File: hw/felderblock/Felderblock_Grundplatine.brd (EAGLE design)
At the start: 100 x 80 mm, 52 parts, among them IC2 LM2936, IC3 ULN2803, IC4 MCP2300X/P, J1 RJ11, J2 RJ11, M1 ARDUINO-NANO-3.0, T2 BC337, X1 TASTENSPERRE1, X2 TASTENSPERRE2, X3 SCHLUESSELSPERRE, X4 I2C, X5 ANSCHALTER

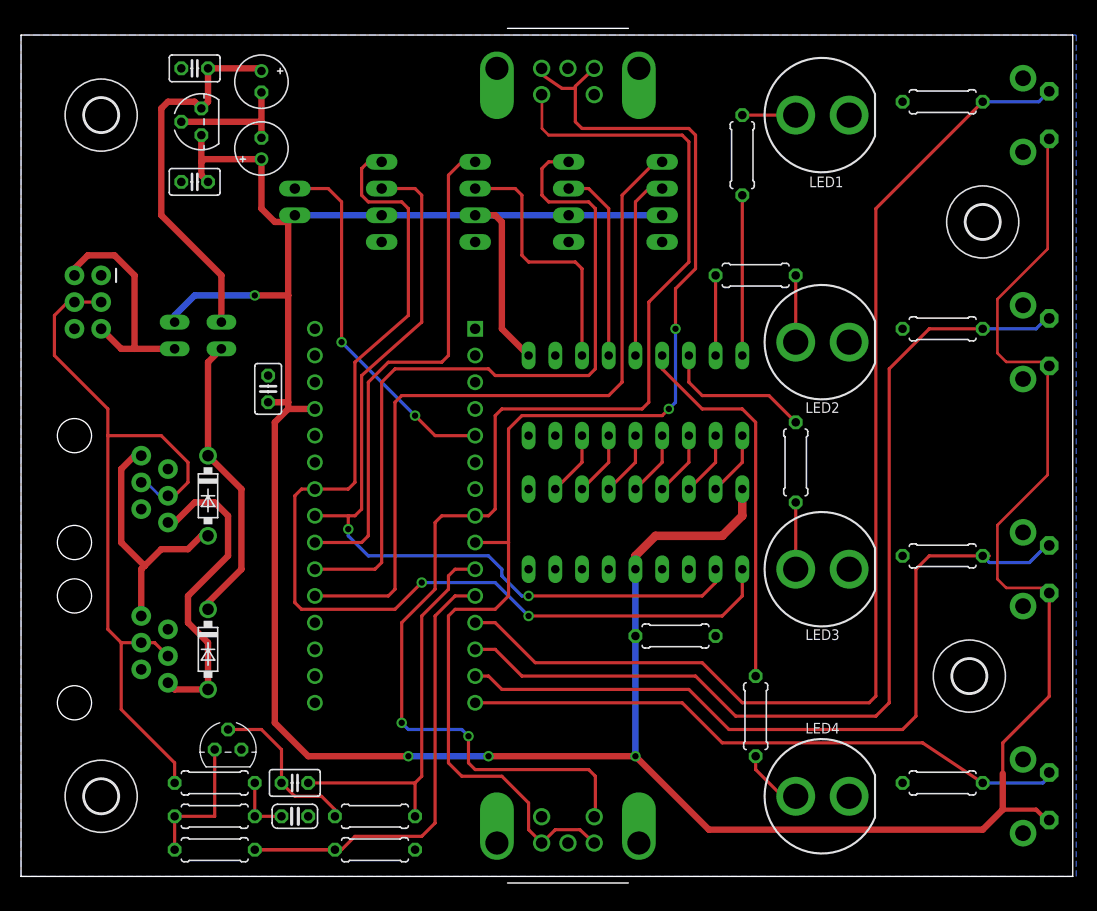
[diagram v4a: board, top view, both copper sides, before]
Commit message: position pcb into housing
restructure parts for housing, made pcb smaller to fit housing, positioned LED and buttons to fit
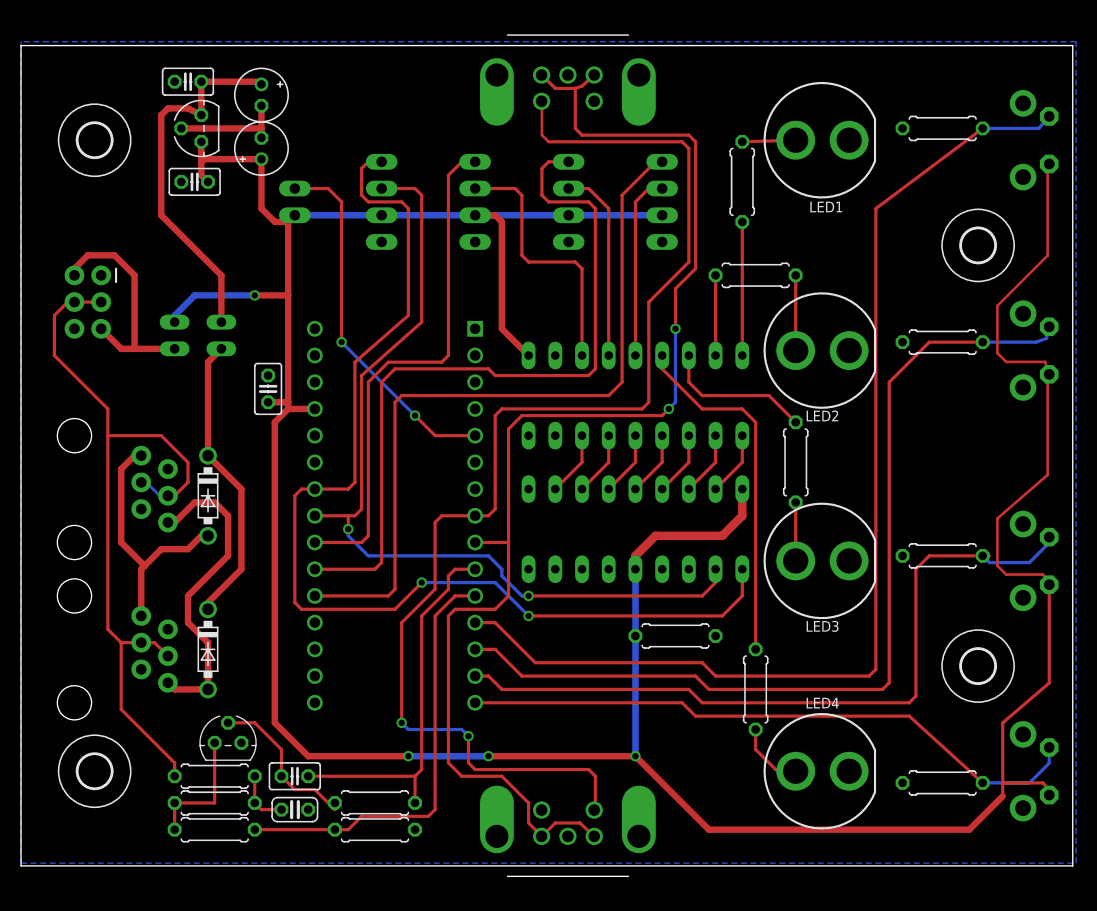
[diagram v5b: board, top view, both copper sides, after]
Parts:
- moved R14 2.54 mm to (69.8, 17.8)
- moved R10 2.54 mm to (87.6, 71.1)
- moved R11 2.54 mm to (68.6, 66.0)
- moved H3 2.47 mm to (7.00, 70.0)
- moved H2 2.46 mm to (7.00, 10.0)
- moved LED1 2.39 mm to (76.2, 70.0)
- moved S1 2.39 mm to (96.5, 70.0)
- moved LED4 2.38 mm to (76.2, 10.0)
- moved S4 2.38 mm to (96.5, 10.0)
- moved H4 2.27 mm to (91.0, 60.0)
- moved R18 1.91 mm to (18.4, 4.45)
- moved R19 1.91 mm to (33.7, 4.45)
- moved C1 1.42 mm to (15.9, 75.6)
- moved R9 1.27 mm to (87.6, 50.8)
- moved R17 1.27 mm to (18.4, 6.99)
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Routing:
- net LN_RX: track 50.1 -> 40.9 mm
- net FELD1_SW: track 109.0 -> 103.8 mm
- net FELD2_SW: track 91.5 -> 87.5 mm
- net +5V: track 325.9 -> 322.9 mm
- net FELD3_SW: track 73.3 -> 70.6 mm
- net FELD4_LEDD: track 36.4 -> 33.9 mm
- net FELD1_LEDD: track 15.2 -> 12.7 mm
- net FELD4_SW: track 57.9 -> 59.8 mm
- net MI_FWD: track 124.3 -> 123.0 mm
- net GND: track 11.9 -> 10.7 mm
- net LN_TX: track 37.1 -> 35.9 mm
- net LN_INTERN: track 13.3 -> 12.1 mm
- net N$7: track 36.3 -> 35.3 mm
- net N$5: track 6.35 -> 7.15 mm
- net N$8: track 6.35 -> 5.56 mm
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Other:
- board size 100 x 80 mm -> 100 x 78 mm
